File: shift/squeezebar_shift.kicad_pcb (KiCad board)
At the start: 2 copper layers, 110 x 18 mm, 54 parts, among them J0 OUTR, J1 PNK, J10 I2C, J11 IDC, J2 RNG, J3 MID, J4 IDX, J5 INNR, J6 THM, J7 XTR, J8 ENCODER, U1 74HC164

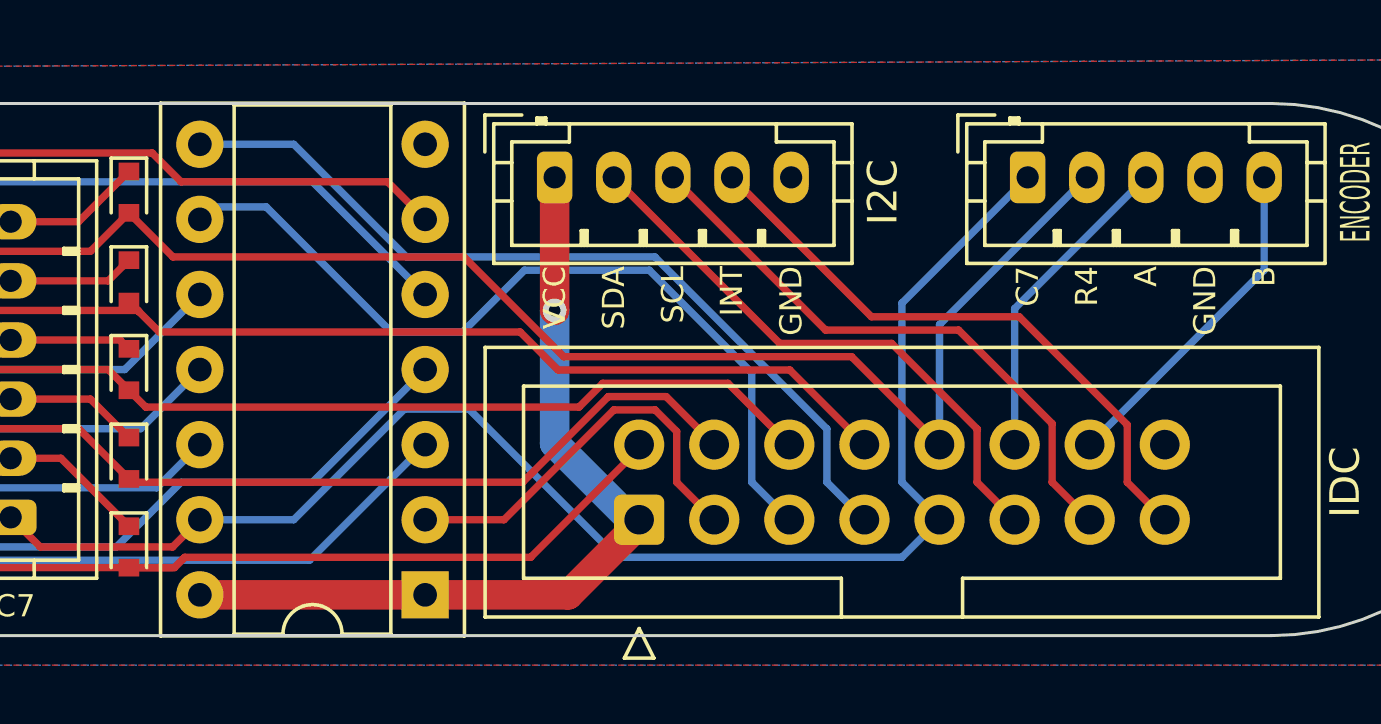
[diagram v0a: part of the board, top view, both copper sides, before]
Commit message: Add labels to Squeezebar-Shift
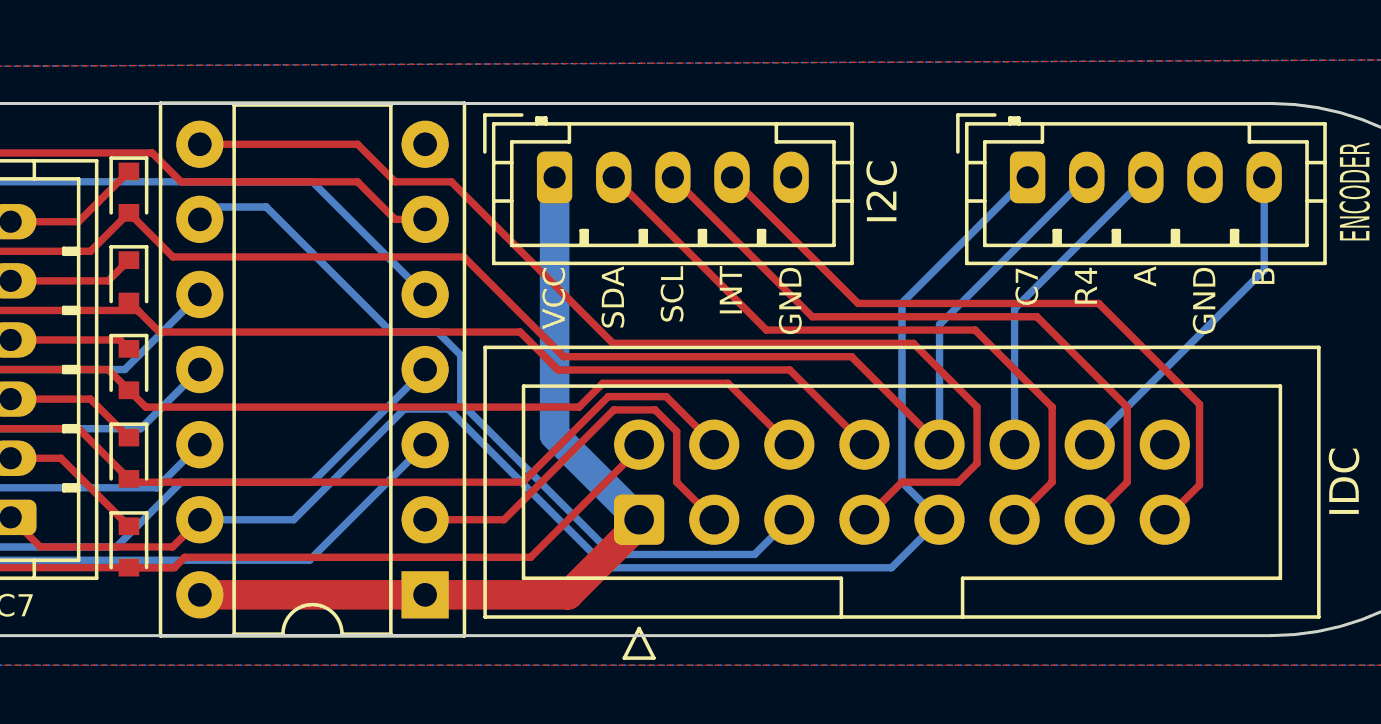
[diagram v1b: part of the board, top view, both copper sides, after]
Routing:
- net /SRCK: track 28.8 -> 36.5 mm
- net /SDA: track 19.4 -> 22.4 mm
- net /SCL: track 20.1 -> 22.9 mm
- net /INT: track 20.6 -> 23.4 mm
- net /SRCLR: track 27.8 -> 25.8 mm
- net VCC: track 28.7 -> 28.8 mm, vias 1 -> 0
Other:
- board text added: "EA"
- board text added: "EB"
- board text added: "G"
- board text added: "SRCK"
- board text added: "SRCR"
- board text added: "SRDA"
- board text added: "SROUT"

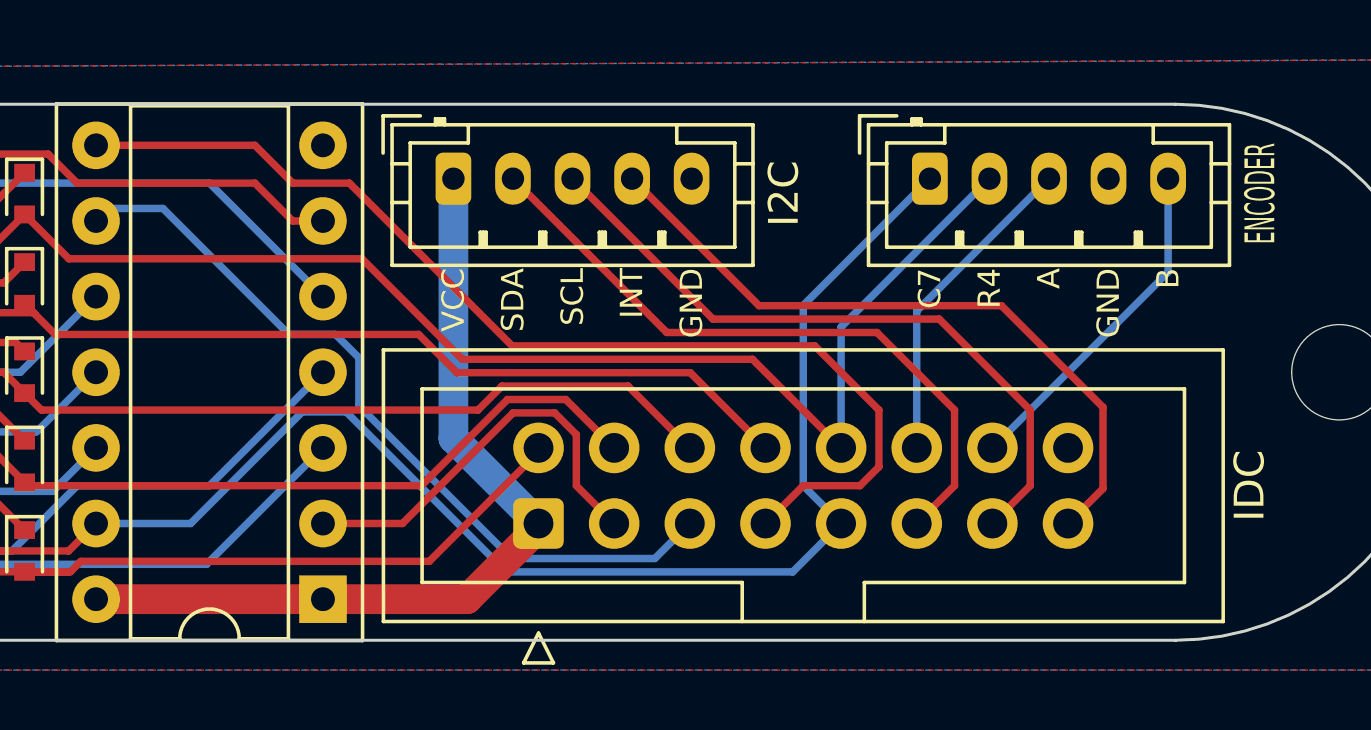
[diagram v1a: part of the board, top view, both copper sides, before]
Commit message: Add SqueezeBarrel
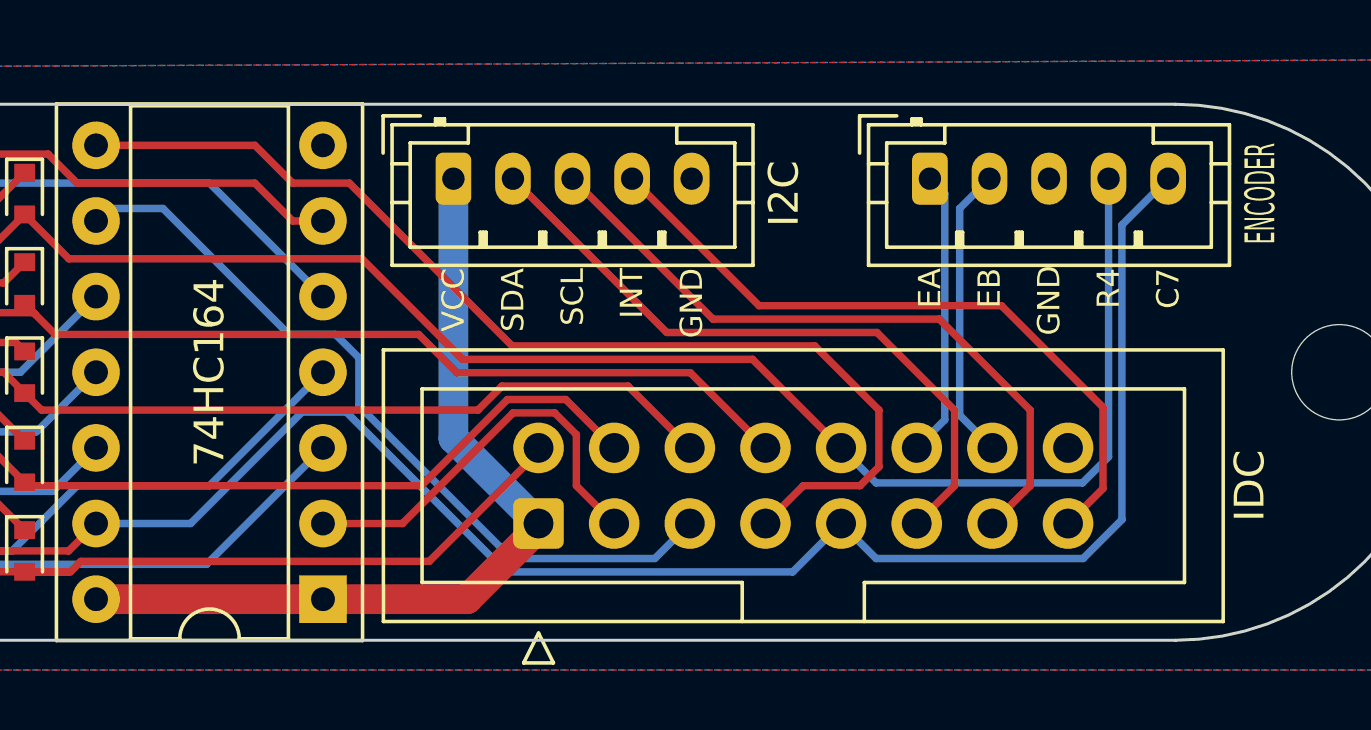
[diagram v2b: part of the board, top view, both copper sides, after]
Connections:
- J8 pad 1: /COL7 -> /ENC_A
- J8 pad 2: /ROW4 -> /ENC_B
- J8 pad 3: /ENC_A -> GND
- J8 pad 4: GND -> /ROW4
- J8 pad 5: /ENC_B -> /COL7
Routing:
- net /COL7: track 50.5 -> 59.2 mm
- net /ROW4: track 98.3 -> 106.4 mm
- net /ENC_B: track 11.5 -> 9.91 mm
- net /ENC_A: track 10.9 -> 9.64 mm
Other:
- board text added: "74HC164"
- board text added: "SQUEEZEBAR:SHIFT 8x5 v1"
- board text removed: "A"
- board text removed: "B"
- board text removed: "SQUEEZEBAR<SHIFT> 8x5 v1"
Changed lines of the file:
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@@
     )
     (pad_to_mask_clearance 0)
-    (grid_origin 167.259 91.08)
+    (grid_origin 160.02 93.62)
     (pcbplotparams
       (layerselection 0x00010fc_ffffffff)
@@
     (fp_line (start 9.95 2.8) (end 9.95 -1.7) (layer "F.Fab") (width 0.1))
     (pad "1" thru_hole roundrect (at 0 0) (size 1.2 1.75) (drill 0.75) (layers *.Cu *.Mask) (roundrect_rratio 0.208333)
-      (net 12 "/COL7") (pinfunction "Pin_1") (pintype "passive"))
+      (net 54 "/ENC_A") (pinfunction "Pin_1") (pintype "passive"))
     (pad "2" thru_hole oval (at 2 0) (size 1.2 1.75) (drill 0.75) (layers *.Cu *.Mask)
-      (net 1 "/ROW4") (pinfunction "Pin_2") (pintype "passive"))
+      (net 56 "/ENC_B") (pinfunction "Pin_2") (pintype "passive"))
     (pad "3" thru_hole oval (at 4 0) (size 1.2 1.75) (drill 0.75) (layers *.Cu *.Mask)
-      (net 54 "/ENC_A") (pinfunction "Pin_3") (pintype "passive"))
+      (net 55 "GND") (pinfunction "Pin_3") (pintype "passive"))
     (pad "4" thru_hole oval (at 6 0) (size 1.2 1.75) (drill 0.75) (layers *.Cu *.Mask)
-      (net 55 "GND") (pinfunction "Pin_4") (pintype "passive"))
+      (net 1 "/ROW4") (pinfunction "Pin_4") (pintype "passive"))
     (pad "5" thru_hole oval (at 8 0) (size 1.2 1.75) (drill 0.75) (layers *.Cu *.Mask)
-      (net 56 "/ENC_B") (pinfunction "Pin_5") (pintype "passive"))
+      (net 12 "/COL7") (pinfunction "Pin_5") (pintype "passive"))
     (model "${KICAD6_3DMODEL_DIR}/Connector_JST.3dshapes/JST_PH_B5B-PH-K_1x05_P2.00mm_Vertical.wrl"
       (offset (xyz 0 0 0))
@@
       (effects (font (size 1 1) (thickness 0.15)))
     )
-    (fp_text value "74HC164" (at 3.81 17.57) (layer "F.Fab")
+    (fp_text value "74HC164" (at 3.81 7.62 90) (layer "F.Fab")
       (effects (font (size 1 1) (thickness 0.15)))
     )
@@
     (effects (font (size 0.75 0.75) (thickness 0.15)) (justify mirror))
   )
-  (gr_text "EB" (at 188.468 78.126) (layer "B.SilkS")
+  (gr_text "EB" (at 182.4 78.126) (layer "B.SilkS")
     (effects (font (size 0.5 0.5) (thickness 0.1)) (justify mirror))
   )
@@
     (effects (font (size 0.75 0.75) (thickness 0.15)) (justify mirror))
   )
-  (gr_text "EA" (at 184.404 78.126) (layer "B.SilkS")
+  (gr_text "EA" (at 180.4 78.126) (layer "B.SilkS")
     (effects (font (size 0.5 0.5) (thickness 0.1)) (justify mirror))
   )
@@
     (effects (font (size 0.75 0.75) (thickness 0.15)) (justify right mirror))
   )
-  (gr_text "R4" (at 182.372 78.126) (layer "B.SilkS")
+  (gr_text "R4" (at 186.4 78.126) (layer "B.SilkS")
     (effects (font (size 0.5 0.5) (thickness 0.1)) (justify mirror))
   )
@@
     (effects (font (size 0.5 0.5) (thickness 0.1)) (justify mirror))
   )
-  (gr_text "C7" (at 180.467 78.126) (layer "B.SilkS")
+  (gr_text "C7" (at 188.4 78.126) (layer "B.SilkS")
     (effects (font (size 0.5 0.5) (thickness 0.1)) (justify mirror))
   )
@@
     (effects (font (size 0.75 0.75) (thickness 0.15)) (justify right mirror))
   )
-  (gr_text "GND" (at 186.436 78.126) (layer "B.SilkS")
+  (gr_text "GND" (at 184.4 78.126) (layer "B.SilkS")
     (effects (font (size 0.5 0.5) (thickness 0.1)) (justify mirror))
   )
@@
     (effects (font (size 0.75 0.75) (thickness 0.15)) (justify left mirror))
   )
-  (gr_text "SQUEEZEBAR<SHIFT> 8x5 v1" (at 175.25 83.46) (layer "B.SilkS")
+  (gr_text "SQUEEZEBAR:SHIFT 8x5 v1" (at 175.25 83.46) (layer "B.SilkS")
     (effects (font (size 4 1) (thickness 0.15)) (justify mirror))
   )
@@
     (effects (font (size 0.75 0.75) (thickness 0.15)) (justify right mirror))
   )
-  (gr_text "B" (at 188.4 82.5 90) (layer "F.SilkS")
+  (gr_text "EB" (at 182.4 82.5 90) (layer "F.SilkS")
     (effects (font (size 0.75 0.75) (thickness 0.15)) (justify right))
   )
@@
     (effects (font (size 1 1) (thickness 0.15)))
   )
-  (gr_text "R4" (at 182.4 82.5 90) (layer "F.SilkS")
+  (gr_text "R4" (at 186.4 82.5 90) (layer "F.SilkS")
     (effects (font (size 0.75 0.75) (thickness 0.15)) (justify right))
   )
@@
     (effects (font (size 0.75 0.75) (thickness 0.15)) (justify right))
   )
-  (gr_text "A" (at 184.4 82.5 90) (layer "F.SilkS")
+  (gr_text "EA" (at 180.4 82.5 90) (layer "F.SilkS")
     (effects (font (size 0.75 0.75) (thickness 0.15)) (justify right))
   )
@@
     (effects (font (size 0.75 0.75) (thickness 0.15)) (justify right))
   )
-  (gr_text "GND" (at 186.4 82.5 90) (layer "F.SilkS")
+  (gr_text "GND" (at 184.4 82.41 90) (layer "F.SilkS")
     (effects (font (size 0.75 0.75) (thickness 0.15)) (justify right))
   )
-  (gr_text "C7" (at 180.4 82.5 90) (layer "F.SilkS")
+  (gr_text "C7" (at 188.4 82.5 90) (layer "F.SilkS")
     (effects (font (size 0.75 0.75) (thickness 0.15)) (justify right))
   )
@@
     (effects (font (size 0.75 0.75) (thickness 0.15)))
   )
+  (gr_text "74HC164" (at 156.21 86 90) (layer "F.SilkS")
+    (effects (font (size 1 1) (thickness 0.15)))
+  )
   (gr_text "2" (at 93.9 85 90) (layer "F.SilkS")
     (effects (font (size 1 1) (thickness 0.15)))
@@
   (segment (start 161.331 82.19) (end 164.706 85.565) (width 0.25) (layer "F.Cu") (net 1))
   (segment (start 115 80.7) (end 116.3 82) (width 0.25) (layer "F.Cu") (net 1))
-  (segment (start 177.419 84.481) (end 182.4 79.5) (width 0.25) (layer "B.Cu") (net 1))
-  (segment (start 177.419 88.54) (end 177.419 84.481) (width 0.25) (layer "B.Cu") (net 1))
+  (segment (start 177.419 88.54) (end 178.594 89.715) (width 0.25) (layer "B.Cu") (net 1))
+  (segment (start 185.525701 89.715) (end 186.4 88.840701) (width 0.25) (layer "B.Cu") (net 1))
+  (segment (start 178.594 89.715) (end 185.525701 89.715) (width 0.25) (layer "B.Cu") (net 1))
+  (segment (start 186.4 88.840701) (end 186.4 79.5) (width 0.25) (layer "B.Cu") (net 1))
   (segment (start 163.59 92.35) (end 167.4 88.54) (width 0.25) (layer "F.Cu") (net 2))
   (segment (start 136 92.7) (end 129 92.7) (width 0.25) (layer "F.Cu") (net 2))
@@
   (segment (start 146 91) (end 147 92) (width 0.25) (layer "F.Cu") (net 12))
   (segment (start 151.48 92) (end 152.4 91.08) (width 0.25) (layer "F.Cu") (net 12))
+  (segment (start 186.85 90.95) (end 185.545 92.255) (width 0.25) (layer "B.Cu") (net 12))
   (segment (start 155.576396 91.08) (end 159.320698 87.335698) (width 0.25) (layer "B.Cu") (net 12))
   (segment (start 166.173604 92.705) (end 175.794 92.705) (width 0.25) (layer "B.Cu") (net 12))
-  (segment (start 176.149 89.81) (end 177.419 91.08) (width 0.25) (layer "B.Cu") (net 12))
+  (segment (start 178.594 92.255) (end 177.419 91.08) (width 0.25) (layer "B.Cu") (net 12))
+  (segment (start 186.85 81.05) (end 186.85 90.95) (width 0.25) (layer "B.Cu") (net 12))
+  (segment (start 185.545 92.255) (end 178.594 92.255) (width 0.25) (layer "B.Cu") (net 12))
   (segment (start 152.4 91.08) (end 155.576396 91.08) (width 0.25) (layer "B.Cu") (net 12))
-  (segment (start 176.149 83.751) (end 180.4 79.5) (width 0.25) (layer "B.Cu") (net 12))
+  (segment (start 188.4 79.5) (end 186.85 81.05) (width 0.25) (layer "B.Cu") (net 12))
   (segment (start 175.794 92.705) (end 177.419 91.08) (width 0.25) (layer "B.Cu") (net 12))
-  (segment (start 176.149 83.751) (end 176.149 89.81) (width 0.25) (layer "B.Cu") (net 12))
   (segment (start 160.804302 87.335698) (end 166.173604 92.705) (width 0.25) (layer "B.Cu") (net 12))
   (segment (start 159.320698 87.335698) (end 160.804302 87.335698) (width 0.25) (layer "B.Cu") (net 12))
@@
   (segment (start 148.3 81) (end 150 79.3) (width 0.25) (layer "F.Cu") (net 53))
   (segment (start 146 81) (end 148.3 81) (width 0.25) (layer "F.Cu") (net 53))
-  (segment (start 179.959 88.54) (end 179.959 83.941) (width 0.25) (layer "B.Cu") (net 54))
-  (segment (start 179.959 83.941) (end 184.4 79.5) (width 0.25) (layer "B.Cu") (net 54))
-  (segment (start 188.4 82.639) (end 188.4 79.5) (width 0.25) (layer "B.Cu") (net 56))
-  (segment (start 182.499 88.54) (end 188.4 82.639) (width 0.25) (layer "B.Cu") (net 56))
+  (segment (start 180.9 80) (end 180.4 79.5) (width 0.25) (layer "B.Cu") (net 54))
+  (segment (start 180.9 87.599) (end 180.9 80) (width 0.25) (layer "B.Cu") (net 54))
+  (segment (start 179.959 88.54) (end 180.9 87.599) (width 0.25) (layer "B.Cu") (net 54))
+  (segment (start 181.4 87.441) (end 181.4 80.5) (width 0.25) (layer "B.Cu") (net 56))
+  (segment (start 182.499 88.54) (end 181.4 87.441) (width 0.25) (layer "B.Cu") (net 56))
+  (segment (start 181.4 80.5) (end 182.4 79.5) (width 0.25) (layer "B.Cu") (net 56))
   (segment (start 152.4 93.62) (end 160.02 93.62) (width 1) (layer "F.Cu") (net 57))
   (segment (start 164.86 93.62) (end 167.4 91.08) (width 1) (layer "F.Cu") (net 57))
